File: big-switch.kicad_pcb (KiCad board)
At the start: 2 copper layers, 76.2 x 76.2 mm, 5 parts, among them J1 Conn_01x07_Socket, SW1 SW_Push, U1 ProMicro

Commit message: routing ocmplete
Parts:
- added SW2: RotaryEncoder_Switch, Keebio-Parts:RotaryEncoder_EC11B-Horizontal-Dual, F.Cu at (89.5, 121.9)
- added SW3: RotaryEncoder_Switch, Keebio-Parts:RotaryEncoder_EC11B-Horizontal-Dual, F.Cu at (136.8, 122.0)
- J1: value Conn_01x07_Socket -> Conn_01x08_Socket; footprint Connector_PinHeader_2.54mm:PinHeader_1x07_P2.54mm_Horizontal -> Connector_PinHeader_2.54mm:PinHeader_1x08_P2.54mm_Horizontal
- U1: value ProMicro -> LonganNano
- moved J2 77.5 mm to (80.0, 62.7), turned to 90 degrees
- moved J1 67.1 mm to (122.0, 120.2), turned to -90 degrees
- moved LS1 50.6 mm to (93.0, 88.1), turned to 90 degrees
- moved U1 30.0 mm to (131.5, 73.0)
- moved SW1 11.5 mm to (113.1, 88.1)
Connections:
- J1 pad 2: VCC -> +3V3
- J1 pad 5: DISP_DC -> unconnected-(J1-Pin_5-Pad5)
- J1 pad 6: DISP_CS -> DISP_DC
- J1 pad 7: DISP_BL -> DISP_CS
- U1 pad 1: unconnected-(U1-TX0/PD3-Pad1) -> +5V
- U1 pad 10: unconnected-(U1-7/PE6-Pad10) -> ENC2_SW
- U1 pad 12: unconnected-(U1-9/PB5-Pad12) -> SCL
- U1 pad 13: unconnected-(U1-10/PB6-Pad13) -> SDA
- U1 pad 16: unconnected-(U1-15/PB1-Pad16) -> GND
- U1 pad 17: unconnected-(U1-A0/PF7-Pad17) -> GND
- U1 pad 2: unconnected-(U1-RX1/PD2-Pad2) -> +3V3
- U1 pad 20: unconnected-(U1-A3/PF4-Pad20) -> DISP_BL
- U1 pad 21: unconnected-(U1-VCC-Pad21) -> DISP_CS
- U1 pad 22: unconnected-(U1-RST-Pad22) -> DISP_DC
- U1 pad 24: unconnected-(U1-RAW-Pad24) -> AUDIO
- U1 pad 25: (no net) -> unconnected-(U1-A3-Pad25)
- U1 pad 26: (no net) -> VIK_CS
- U1 pad 27: (no net) -> SCLK
- U1 pad 28: (no net) -> MISO
- U1 pad 29: (no net) -> MOSI
- U1 pad 3: unconnected-(U1-GND-Pad3) -> SW_1
- U1 pad 30: (no net) -> GPIO_X2
- U1 pad 31: (no net) -> GPIO_X1
- U1 pad 32: (no net) -> VIK_RGB
- U1 pad 33: (no net) -> unconnected-(U1-B11-Pad33)
- U1 pad 34: (no net) -> unconnected-(U1-RST-Pad34)
- U1 pad 5: unconnected-(U1-2/PD1-Pad5) -> ENC1_A
- U1 pad 6: unconnected-(U1-3/PD0-Pad6) -> ENC1_B
- U1 pad 7: unconnected-(U1-4/PD4-Pad7) -> ENC1_SW
- U1 pad 8: unconnected-(U1-5/PC6-Pad8) -> ENC2_A
- U1 pad 9: unconnected-(U1-6/PD7-Pad9) -> ENC2_B
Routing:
- net +3V3: track 0.00 -> 116.0 mm, vias 0 -> 4
- net SCL: track 0.00 -> 109.6 mm, vias 0 -> 5
- net SDA: track 0.00 -> 108.7 mm, vias 0 -> 5
- net ENC1_A: track 0.00 -> 88.3 mm, vias 0 -> 4
- net SCLK: track 0.00 -> 86.5 mm, vias 0 -> 2
- net MISO: track 0.00 -> 85.8 mm, vias 0 -> 2
- net ENC1_B: track 0.00 -> 85.7 mm, vias 0 -> 4
- net ENC1_SW: track 0.00 -> 85.3 mm, vias 0 -> 3
- net VIK_CS: track 0.00 -> 79.5 mm, vias 0 -> 1
- net MOSI: track 0.00 -> 74.5 mm, vias 0 -> 3
- net DISP_DC: track 0.00 -> 69.8 mm, vias 0 -> 2
- net DISP_CS: track 0.00 -> 68.9 mm, vias 0 -> 2
- net DISP_BL: track 0.00 -> 66.0 mm, vias 0 -> 2
- net ENC2_B: track 0.00 -> 65.7 mm, vias 0 -> 1
- net GPIO_X2: track 0.00 -> 65.5 mm, vias 0 -> 3
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- added copper zone on B.Cu, net GND
- added copper zone on F.Cu, net GND

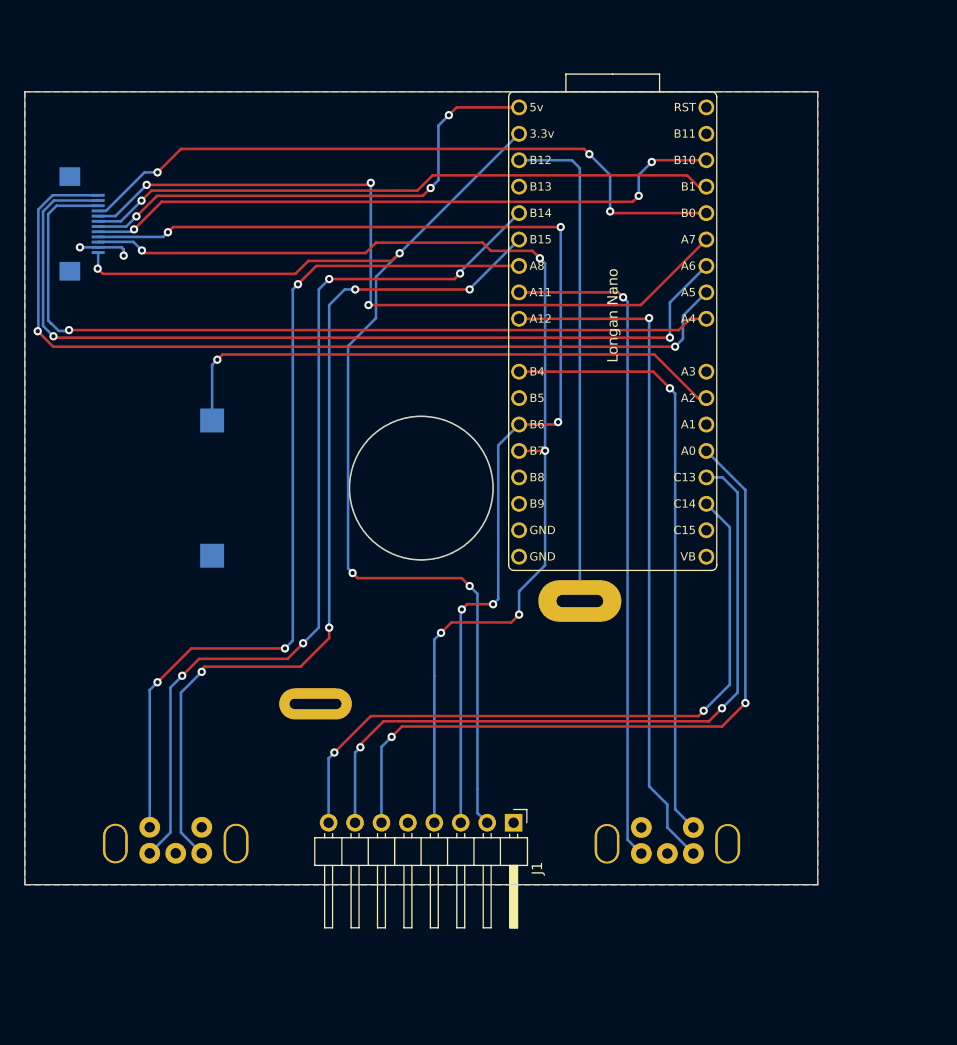
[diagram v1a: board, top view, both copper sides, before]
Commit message: flipped mcu side, rerouted
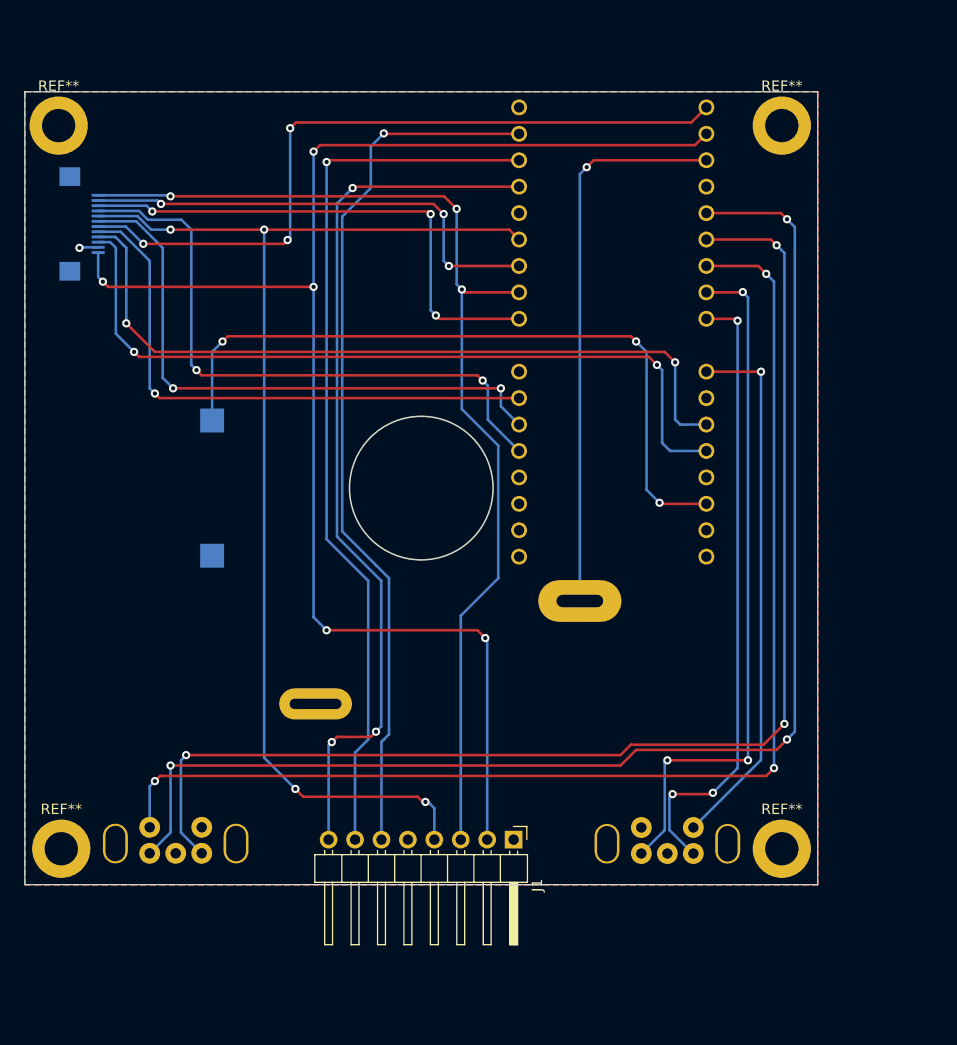
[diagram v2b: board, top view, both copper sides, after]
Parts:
- added REF**: MountingHole_3.2mm_M3_DIN965_Pad, MountingHole:MountingHole_3.2mm_M3_DIN965_Pad, F.Cu at (78.2, 53.2)
- added REF**: MountingHole_3.2mm_M3_DIN965_Pad, MountingHole:MountingHole_3.2mm_M3_DIN965_Pad, F.Cu at (147.8, 122.8)
- added REF**: MountingHole_3.2mm_M3_DIN965_Pad, MountingHole:MountingHole_3.2mm_M3_DIN965_Pad, F.Cu at (78.5, 122.8)
- added REF**: MountingHole_3.2mm_M3_DIN965_Pad, MountingHole:MountingHole_3.2mm_M3_DIN965_Pad, F.Cu at (147.8, 53.2)
- J1: value Conn_01x08_Socket -> Conn_01x07_Socket
- U1: moved to B.Cu
- moved J1 1.62 mm to (122.0, 121.9)
- turned U1 to 180 degrees
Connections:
- J1 pad 3: SCL -> SCLK
- J1 pad 4: SDA -> MOSI
- U1 pad 15: unconnected-(U1-B9-Pad15) -> AUDIO
- U1 pad 20: DISP_BL -> unconnected-(U1-C14-Pad20)
- U1 pad 21: DISP_CS -> unconnected-(U1-C13-Pad21)
- U1 pad 22: DISP_DC -> GPIO_X2
- U1 pad 23: unconnected-(U1-A1-Pad23) -> GPIO_X1
- U1 pad 24: AUDIO -> VIK_RGB
- U1 pad 30: GPIO_X2 -> unconnected-(U1-B0-Pad30)
- U1 pad 31: GPIO_X1 -> DISP_BL
- U1 pad 32: VIK_RGB -> DISP_CS
- U1 pad 33: unconnected-(U1-B11-Pad33) -> DISP_DC
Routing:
- net MISO: track 85.8 -> 45.7 mm, vias 2 -> 3
- net ENC1_A: track 88.3 -> 128.2 mm, vias 4 -> 3
- net MOSI: track 74.5 -> 113.5 mm, vias 3 -> 4
- net ENC1_B: track 85.7 -> 122.5 mm, vias 4 -> 3
- net SCL: track 109.6 -> 73.4 mm, vias 5 -> 2
- net ENC1_SW: track 85.3 -> 118.5 mm
- net SDA: track 108.7 -> 75.7 mm, vias 5 -> 2
- net VIK_CS: track 79.5 -> 50.4 mm, vias 1 -> 3
- net +3V3: track 116.0 -> 143.4 mm, vias 4 -> 5
- net +5V: track 48.3 -> 70.7 mm
- net DISP_BL: track 66.0 -> 85.1 mm, vias 2 -> 3
- net SCLK: track 86.5 -> 104.4 mm, vias 2 -> 3
- net DISP_CS: track 68.9 -> 85.9 mm, vias 2 -> 1
- net DISP_DC: track 69.8 -> 84.7 mm, vias 2 -> 1
- net AUDIO: track 55.0 -> 69.1 mm, vias 1 -> 3
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
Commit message: rounded corners
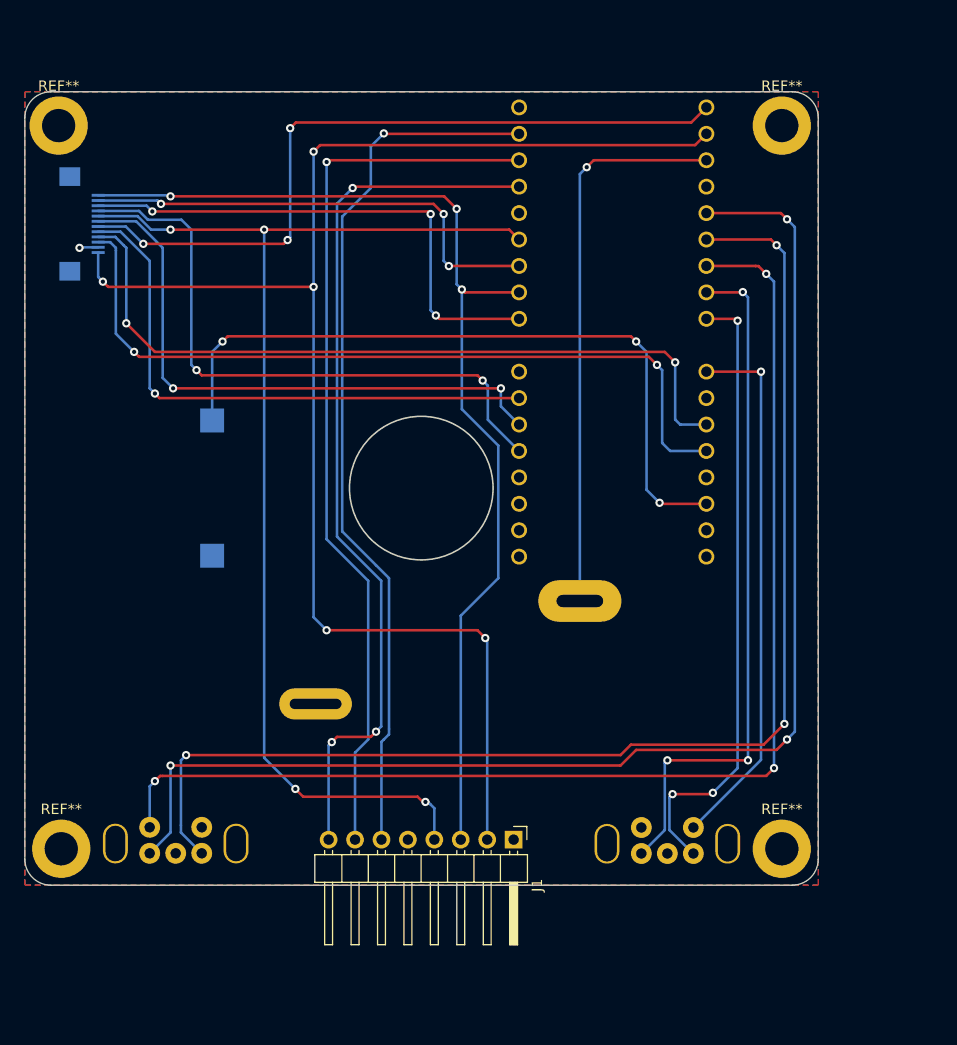
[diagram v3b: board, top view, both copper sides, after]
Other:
- outline, holes or cut-outs redrawn
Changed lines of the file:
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@@
       (outputformat 1)
       (mirror false)
-      (drillshape 1)
+      (drillshape 0)
       (scaleselection 1)
-      (outputdirectory "")
+      (outputdirectory "gerbers/")
     )
   )
@@
     )
   )
-  (gr_line (start 75 50) (end 151.2 50)
+  (gr_line (start 148.75 126.25) (end 77.5 126.25)
     (stroke (width 0.1) (type default)) (layer "Edge.Cuts"))
-  (gr_line (start 75 126.2) (end 75 50)
+  (gr_line (start 77.5 50) (end 148.75 50)
     (stroke (width 0.1) (type default)) (layer "Edge.Cuts"))
-  (gr_line (start 151.2 50) (end 151.2 126.2)
+  (gr_arc (start 148.75 50) (mid 150.517767 50.732233) (end 151.25 52.5)
     (stroke (width 0.1) (type default)) (layer "Edge.Cuts"))
-  (gr_line (start 151.2 126.2) (end 75 126.2)
+  (gr_line (start 151.25 52.5) (end 151.25 123.75)
+    (stroke (width 0.1) (type default)) (layer "Edge.Cuts"))
+  (gr_arc (start 77.5 126.25) (mid 75.732233 125.517767) (end 75 123.75)
+    (stroke (width 0.1) (type default)) (layer "Edge.Cuts"))
+  (gr_line (start 75 123.75) (end 75 52.5)
+    (stroke (width 0.1) (type default)) (layer "Edge.Cuts"))
+  (gr_arc (start 151.25 123.75) (mid 150.517767 125.517767) (end 148.75 126.25)
+    (stroke (width 0.1) (type default)) (layer "Edge.Cuts"))
+  (gr_arc (start 75 52.5) (mid 75.732233 50.732233) (end 77.5 50)
     (stroke (width 0.1) (type default)) (layer "Edge.Cuts"))
   (via (at 80.25 65) (size 0.8) (drill 0.4) (layers "F.Cu" "B.Cu") (net 1))

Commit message: added LED
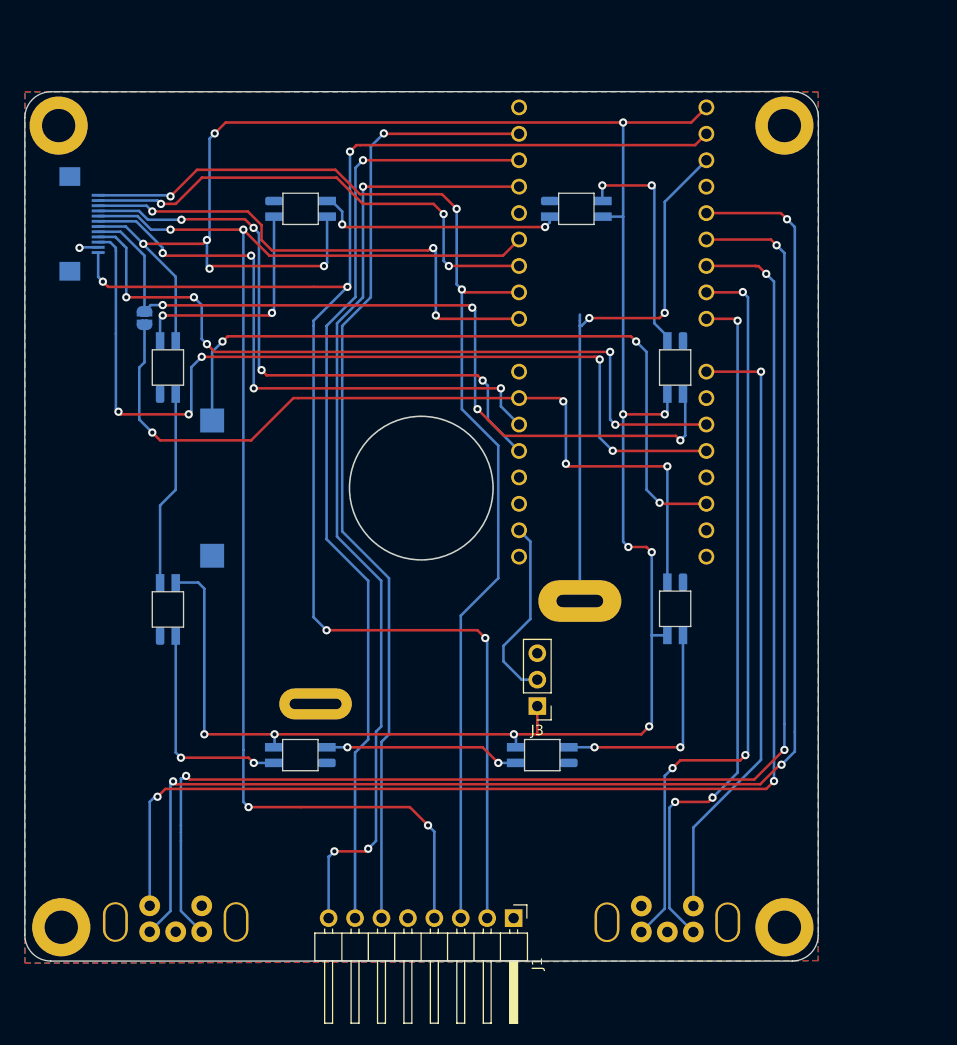
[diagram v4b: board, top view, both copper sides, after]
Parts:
- added D1: SK6812MINI-E, Keebio-Parts:SK6812-MINI-E, B.Cu at (137.5, 99.7)
- added D2: SK6812MINI-E, Keebio-Parts:SK6812-MINI-E, B.Cu at (124.7, 113.8)
- added D3: SK6812MINI-E, Keebio-Parts:SK6812-MINI-E, B.Cu at (101.5, 113.8)
- added D4: SK6812MINI-E, Keebio-Parts:SK6812-MINI-E, B.Cu at (88.8, 99.8)
- added D5: SK6812MINI-E, Keebio-Parts:SK6812-MINI-E, B.Cu at (88.8, 76.5)
- added D6: SK6812MINI-E, Keebio-Parts:SK6812-MINI-E, B.Cu at (101.5, 61.2)
- added D7: SK6812MINI-E, Keebio-Parts:SK6812-MINI-E, B.Cu at (128.0, 61.2)
- added D8: SK6812MINI-E, Keebio-Parts:SK6812-MINI-E, B.Cu at (137.5, 76.5)
- added J3: Conn_01x03_Socket, Connector_PinHeader_2.54mm:PinHeader_1x03_P2.54mm_Vertical, F.Cu at (124.2, 109.0)
- added JP1: Jumper_2_Open, Jumper:SolderJumper-2_P1.3mm_Open_RoundedPad1.0x1.5mm, B.Cu at (86.5, 71.8)
- moved REF** 7.55 mm to (148.0, 130.3)
- moved SW3 7.54 mm to (136.8, 129.5)
- moved J1 7.54 mm to (122.0, 129.4)
- moved REF** 7.54 mm to (78.5, 130.3)
- moved SW2 7.54 mm to (89.5, 129.5)
- moved REF** 0.25 mm to (148.0, 53.2)
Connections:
- U1 pad 19: unconnected-(U1-C15-Pad19) -> LED_RING
- U1 pad 24: VIK_RGB -> RGB_DIN
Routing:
- net +5V: track 70.7 -> 234.7 mm, vias 3 -> 14
- net RGB_DIN: track 0.00 -> 79.8 mm, vias 0 -> 4
- net Net-(D6-DOUT): track 0.00 -> 23.9 mm, vias 0 -> 2
- net VIK_RGB: track 54.3 -> 78.0 mm, vias 1 -> 4
- net Net-(D5-DOUT): track 0.00 -> 22.5 mm, vias 0 -> 2
- net Net-(D7-DOUT): track 0.00 -> 21.8 mm, vias 0 -> 2
- net Net-(D1-DOUT): track 0.00 -> 21.6 mm, vias 0 -> 2
- net Net-(D3-DOUT): track 0.00 -> 21.1 mm, vias 0 -> 2
- net Net-(D4-DOUT): track 0.00 -> 18.8 mm
- net Net-(D2-DOUT): track 0.00 -> 18.8 mm, vias 0 -> 2
- net LED_RING: track 0.00 -> 18.1 mm
- net MOSI: track 113.5 -> 125.5 mm
- net SDA: track 75.7 -> 87.3 mm, vias 2 -> 5
- net SCLK: track 104.4 -> 114.0 mm
- net +3V3: track 143.4 -> 152.2 mm
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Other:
- board size 76.2 x 76.2 mm -> 76.3 x 83.6 mm
- board text added: "+5V"
- board text added: "GND"
- board text added: "LED_DOUT"
- board text added: "VIK RGB"

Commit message: updted to support rp2040-zero
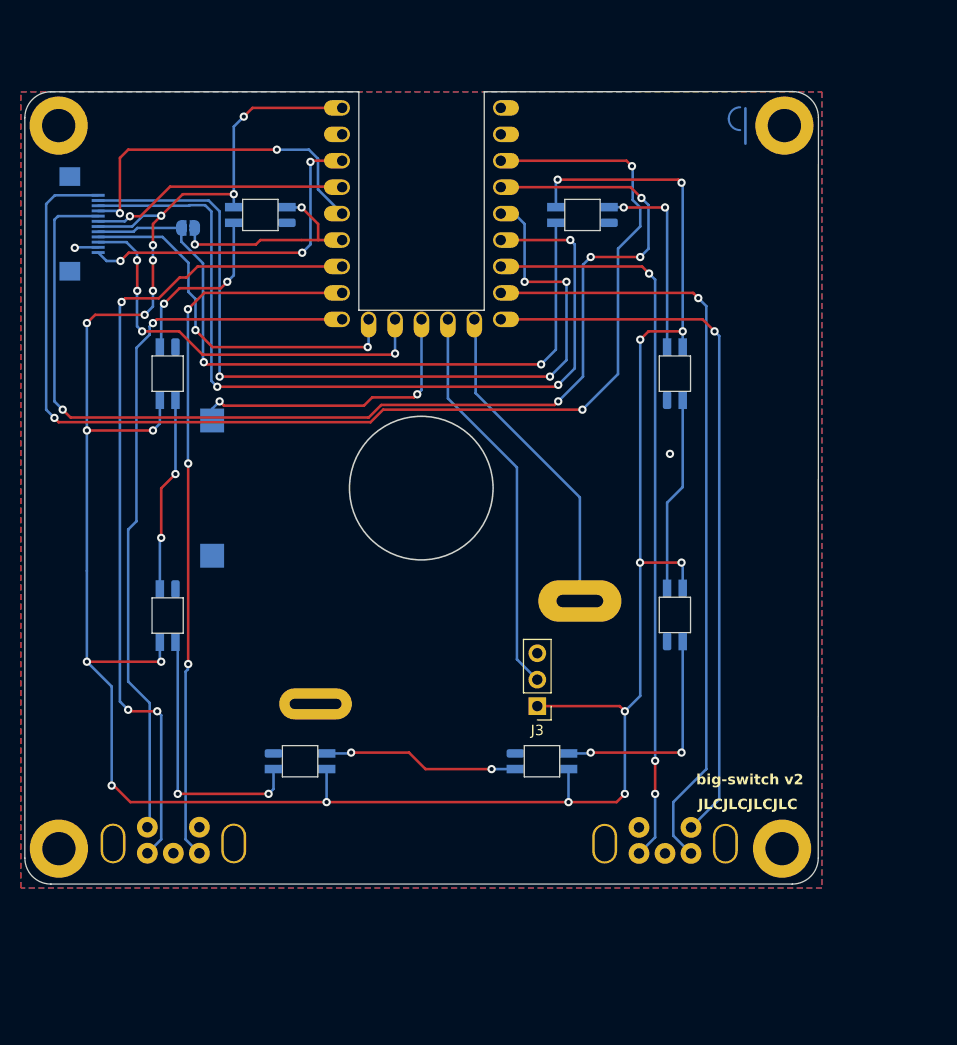
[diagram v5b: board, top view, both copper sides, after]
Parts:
- removed J1: Conn_01x07_Socket, Connector_PinHeader_2.54mm:PinHeader_1x08_P2.54mm_Horizontal
- removed U1: LonganNano, prsid:Longan_Nano
- added G***: LOGO, LOGO, F.Cu at (86.8, 111.0)
- added G***: LOGO, LOGO, B.Cu at (139.8, 111.5)
- added G***: LOGO, LOGO, B.Cu at (137.3, 55.6)
- added U2: rp2040-zero, prsid:rp2040-zero-tht, F.Cu at (113.1, 61.7)
- moved D1 55.0 mm to (97.6, 61.8), turned to 0 degrees
- moved D6 53.1 mm to (137.5, 100.3), turned to -90 degrees
- moved D5 52.2 mm to (124.7, 114.3), turned to 180 degrees
- moved D2 51.4 mm to (88.7, 77.1), turned to 90 degrees
- moved D4 19.3 mm to (101.5, 114.3), turned to 180 degrees
- moved D3 18.5 mm to (88.7, 100.3), turned to 90 degrees
- moved D7 18.5 mm to (137.5, 77.1), turned to -90 degrees
- moved D8 17.2 mm to (128.6, 61.8), turned to 0 degrees
- moved JP1 9.62 mm to (90.7, 63.1), turned to 180 degrees
- moved SW3 7.55 mm to (136.5, 122.0)
- moved REF** 7.55 mm to (147.8, 122.7)
- moved REF** 7.55 mm to (78.3, 122.7)
- moved SW2 7.55 mm to (89.3, 121.9)
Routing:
- net +3V3: track 152.2 -> 32.4 mm, vias 5 -> 3
- net DISP_DC: track 92.3 -> 0.00 mm, vias 1 -> 0
- net DISP_BL: track 92.0 -> 0.00 mm, vias 3 -> 0
- net DISP_CS: track 91.5 -> 0.00 mm, vias 1 -> 0
- net ENC1_B: track 130.8 -> 68.4 mm
- net RGB_DIN: track 79.8 -> 21.1 mm, vias 4 -> 2
- net ENC1_SW: track 125.9 -> 68.9 mm, vias 3 -> 1
- net ENC1_A: track 136.0 -> 79.8 mm
- net SDA: track 87.3 -> 40.4 mm, vias 5 -> 4
- net AUDIO: track 69.1 -> 29.1 mm, vias 3 -> 2
- net SCL: track 74.4 -> 36.4 mm, vias 5 -> 2
- net MISO: track 47.8 -> 81.8 mm, vias 3 -> 4
- net VIK_CS: track 49.6 -> 82.5 mm
- net GPIO_X1: track 57.2 -> 24.9 mm, vias 4 -> 1
- net +5V: track 234.7 -> 264.4 mm, vias 14 -> 23
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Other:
- board size 76.3 x 83.6 mm -> 76.3 x 76.2 mm
- board text added: "JLCJLCJLCJLC"
- board text added: "big-switch v2"
